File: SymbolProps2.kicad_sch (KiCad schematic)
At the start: 3 parts

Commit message: actually aligned correctly
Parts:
- removed U? (x3): PropsTest, symbol PropLib:PropsTest
- added U? (x12): PropsTest, symbol PropLib:PropsTest
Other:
- note added: "+90"
- note added: "-90"
- note added: "180"
- note added: "MIR X"
- note added: "MIR Y"
- note added: "PLAIN"

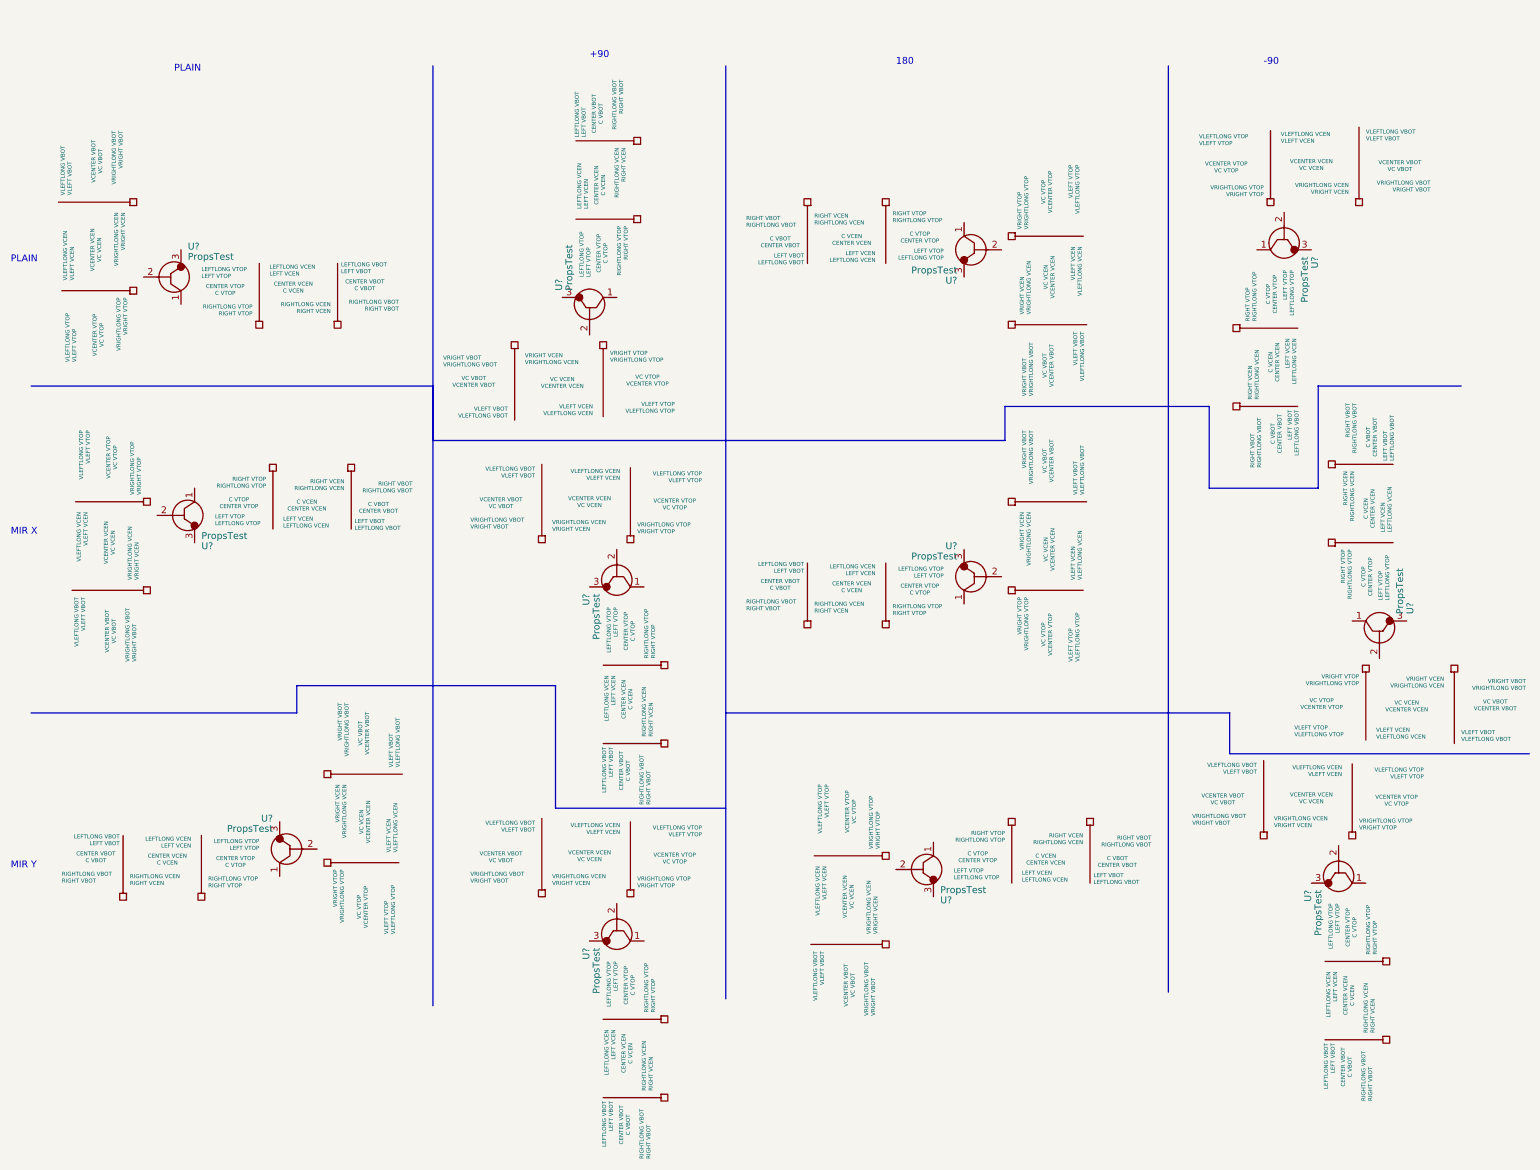
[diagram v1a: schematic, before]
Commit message: add ref annotations
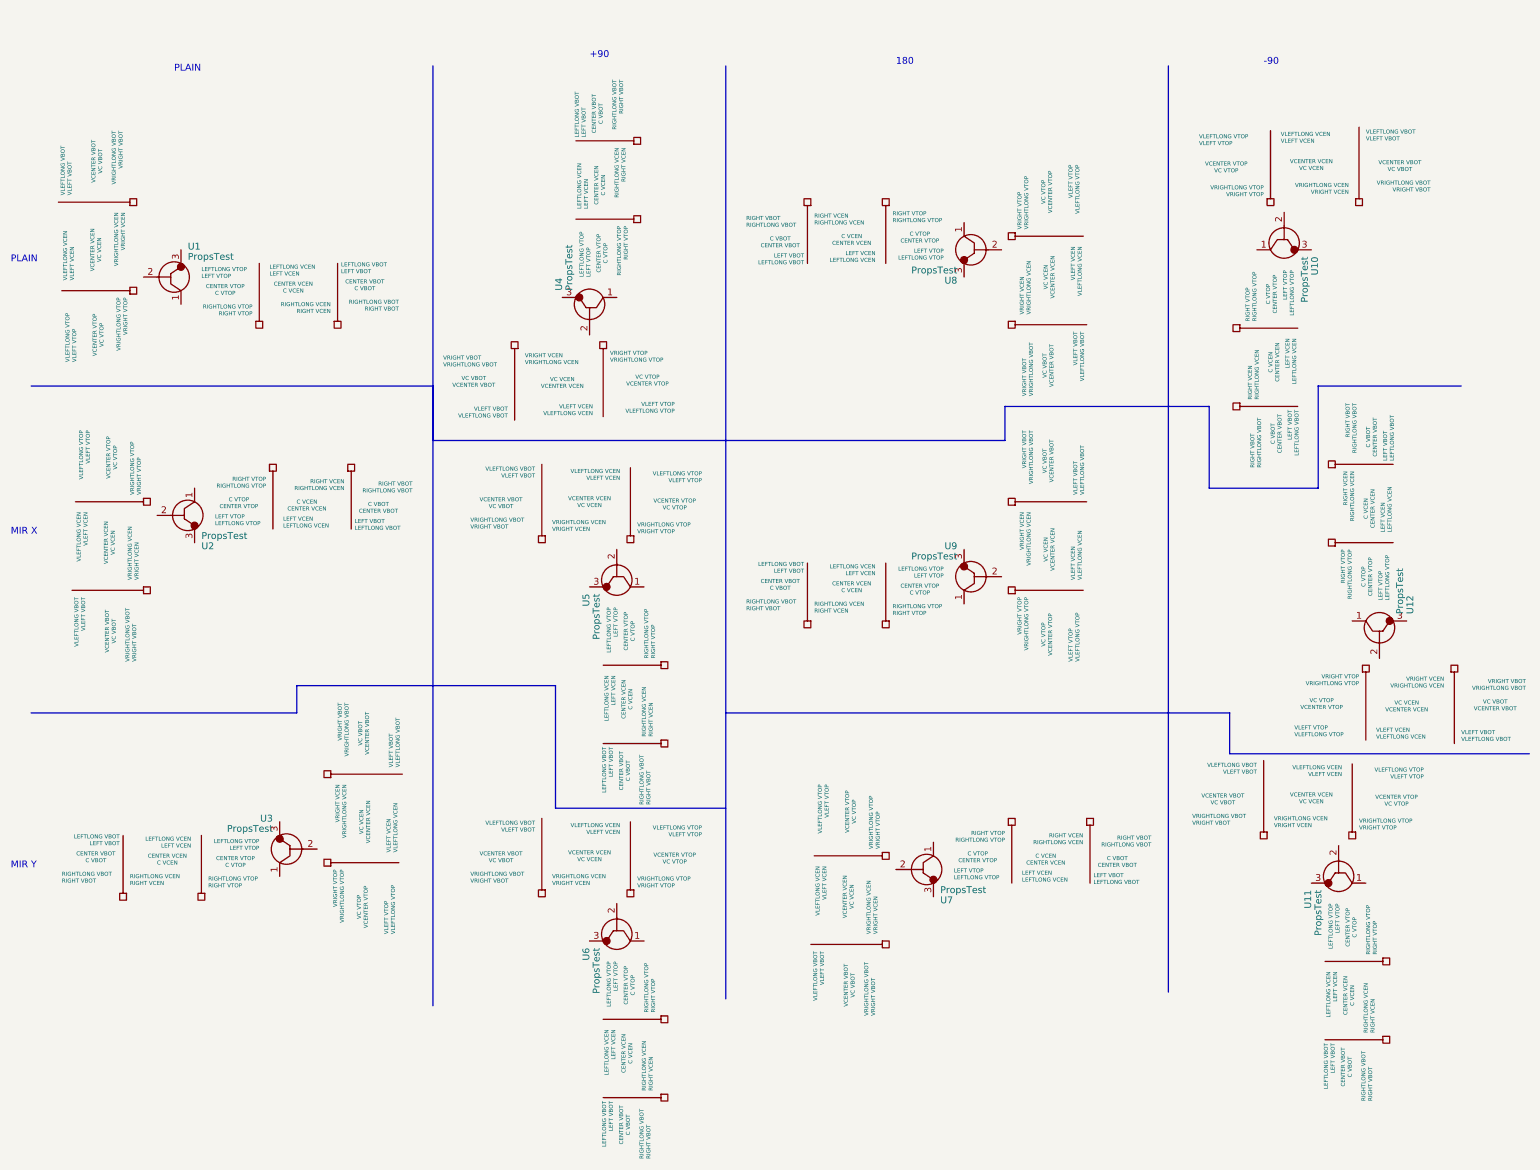
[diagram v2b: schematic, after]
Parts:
- gave numbers to parts that had none: 12
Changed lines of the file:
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@@
   (symbol (lib_id "PropLib:PropsTest") (at 183.515 175.26 0) (mirror x) (unit 1)
     (in_bom yes) (on_board yes)
-    (property "Reference" "U?" (id 0) (at 186.055 175.895 0)
+    (property "Reference" "U7" (id 0) (at 186.055 175.895 0)
       (effects (font (size 1.27 1.27)) (justify left))
     )
@@
   (symbol (lib_id "PropLib:PropsTest") (at 64.135 161.29 0) (mirror y) (unit 1)
     (in_bom yes) (on_board yes)
-    (property "Reference" "U?" (id 0) (at 61.595 160.655 0)
+    (property "Reference" "U3" (id 0) (at 61.595 160.655 0)
       (effects (font (size 1.27 1.27)) (justify left))
     )
@@
   (symbol (lib_id "PropLib:PropsTest") (at 273.05 125.095 270) (mirror x) (unit 1)
     (in_bom yes) (on_board yes)
-    (property "Reference" "U?" (id 0) (at 273.685 122.555 0)
+    (property "Reference" "U12" (id 0) (at 273.685 122.555 0)
       (effects (font (size 1.27 1.27)) (justify left))
     )
@@
   (symbol (lib_id "PropLib:PropsTest") (at 120.65 182.245 90) (mirror x) (unit 1)
     (in_bom yes) (on_board yes)
-    (property "Reference" "U?" (id 0) (at 120.015 184.785 0)
+    (property "Reference" "U6" (id 0) (at 120.015 184.785 0)
       (effects (font (size 1.27 1.27)) (justify left))
     )
@@
   (symbol (lib_id "PropLib:PropsTest") (at 43.18 54.61 0) (unit 1)
     (in_bom yes) (on_board yes)
-    (property "Reference" "U?" (id 0) (at 45.72 53.975 0)
+    (property "Reference" "U1" (id 0) (at 45.72 53.975 0)
       (effects (font (size 1.27 1.27)) (justify left))
     )
@@
   (symbol (lib_id "PropLib:PropsTest") (at 255.27 53.34 270) (unit 1)
     (in_bom yes) (on_board yes)
-    (property "Reference" "U?" (id 0) (at 255.905 55.88 0)
+    (property "Reference" "U10" (id 0) (at 255.905 55.88 0)
       (effects (font (size 1.27 1.27)) (justify left))
     )
@@
   (symbol (lib_id "PropLib:PropsTest") (at 191.77 59.69 180) (unit 1)
     (in_bom yes) (on_board yes)
-    (property "Reference" "U?" (id 0) (at 189.23 60.325 0)
+    (property "Reference" "U8" (id 0) (at 189.23 60.325 0)
       (effects (font (size 1.27 1.27)) (justify left))
     )
@@
   (symbol (lib_id "PropLib:PropsTest") (at 120.65 116.205 90) (mirror x) (unit 1)
     (in_bom yes) (on_board yes)
-    (property "Reference" "U?" (id 0) (at 120.015 118.745 0)
+    (property "Reference" "U5" (id 0) (at 120.015 118.745 0)
       (effects (font (size 1.27 1.27)) (justify left))
     )
@@
   (symbol (lib_id "PropLib:PropsTest") (at 255.27 171.45 90) (mirror x) (unit 1)
     (in_bom yes) (on_board yes)
-    (property "Reference" "U?" (id 0) (at 254.635 173.99 0)
+    (property "Reference" "U11" (id 0) (at 254.635 173.99 0)
       (effects (font (size 1.27 1.27)) (justify left))
     )
@@
   (symbol (lib_id "PropLib:PropsTest") (at 191.77 110.49 0) (mirror y) (unit 1)
     (in_bom yes) (on_board yes)
-    (property "Reference" "U?" (id 0) (at 189.23 109.855 0)
+    (property "Reference" "U9" (id 0) (at 189.23 109.855 0)
       (effects (font (size 1.27 1.27)) (justify left))
     )
@@
   (symbol (lib_id "PropLib:PropsTest") (at 115.57 64.77 90) (unit 1)
     (in_bom yes) (on_board yes)
-    (property "Reference" "U?" (id 0) (at 114.935 62.23 0)
+    (property "Reference" "U4" (id 0) (at 114.935 62.23 0)
       (effects (font (size 1.27 1.27)) (justify left))
     )
@@
   (symbol (lib_id "PropLib:PropsTest") (at 45.72 109.22 0) (mirror x) (unit 1)
     (in_bom yes) (on_board yes)
-    (property "Reference" "U?" (id 0) (at 48.26 109.855 0)
+    (property "Reference" "U2" (id 0) (at 48.26 109.855 0)
       (effects (font (size 1.27 1.27)) (justify left))
     )
@@
   )
   (symbol_instances
+    (path "/607681bc-b8ab-4cc3-bcbe-d5cdf4623d17"
+      (reference "U1") (unit 1) (value "PropsTest") (footprint "")
+    )
+    (path "/d1604d4c-584e-4e63-9761-bccff5ea1220"
+      (reference "U2") (unit 1) (value "PropsTest") (footprint "")
+    )
+    (path "/302a6788-cdde-4eda-bd6a-10393a6c4075"
+      (reference "U3") (unit 1) (value "PropsTest") (footprint "")
+    )
+    (path "/c09b4851-553e-4297-9d60-9ff4a40ae4ee"
+      (reference "U4") (unit 1) (value "PropsTest") (footprint "")
+    )
+    (path "/8722b612-3282-498c-be60-45a7b3205850"
+      (reference "U5") (unit 1) (value "PropsTest") (footprint "")
+    )
+    (path "/5681e071-aff0-4628-ba3c-632cbed13cad"
+      (reference "U6") (unit 1) (value "PropsTest") (footprint "")
+    )
     (path "/29a881e8-06df-4b6b-afb0-3c2df8355293"
-      (reference "U?") (unit 1) (value "PropsTest") (footprint "")
-    )
-    (path "/302a6788-cdde-4eda-bd6a-10393a6c4075"
-      (reference "U?") (unit 1) (value "PropsTest") (footprint "")
+      (reference "U7") (unit 1) (value "PropsTest") (footprint "")
+    )
+    (path "/8285ad37-34fa-4bac-8b4e-ebcb827dd7e3"
+      (reference "U8") (unit 1) (value "PropsTest") (footprint "")
+    )
+    (path "/bd6d4bff-5ad6-4b0b-b3d0-86cdd8ca4399"
+      (reference "U9") (unit 1) (value "PropsTest") (footprint "")
+    )
+    (path "/81611058-008a-4b8d-b0a8-652432d762c0"
+      (reference "U10") (unit 1) (value "PropsTest") (footprint "")
+    )
+    (path "/a431c1e4-6c80-42a2-b56c-6b8cbb3325b1"
+      (reference "U11") (unit 1) (value "PropsTest") (footprint "")
     )
     (path "/3bb5f9d7-3747-4cee-9ede-8fcd24e3d2ab"
-      (reference "U?") (unit 1) (value "PropsTest") (footprint "")
-    )
-    (path "/5681e071-aff0-4628-ba3c-632cbed13cad"
-      (reference "U?") (unit 1) (value "PropsTest") (footprint "")
-    )
-    (path "/607681bc-b8ab-4cc3-bcbe-d5cdf4623d17"
-      (reference "U?") (unit 1) (value "PropsTest") (footprint "")
-    )
-    (path "/81611058-008a-4b8d-b0a8-652432d762c0"
-      (reference "U?") (unit 1) (value "PropsTest") (footprint "")
-    )
-    (path "/8285ad37-34fa-4bac-8b4e-ebcb827dd7e3"
-      (reference "U?") (unit 1) (value "PropsTest") (footprint "")
-    )
-    (path "/8722b612-3282-498c-be60-45a7b3205850"
-      (reference "U?") (unit 1) (value "PropsTest") (footprint "")
-    )
-    (path "/a431c1e4-6c80-42a2-b56c-6b8cbb3325b1"
-      (reference "U?") (unit 1) (value "PropsTest") (footprint "")
-    )
-    (path "/bd6d4bff-5ad6-4b0b-b3d0-86cdd8ca4399"
-      (reference "U?") (unit 1) (value "PropsTest") (footprint "")
-    )
-    (path "/c09b4851-553e-4297-9d60-9ff4a40ae4ee"
-      (reference "U?") (unit 1) (value "PropsTest") (footprint "")
-    )
-    (path "/d1604d4c-584e-4e63-9761-bccff5ea1220"
-      (reference "U?") (unit 1) (value "PropsTest") (footprint "")
+      (reference "U12") (unit 1) (value "PropsTest") (footprint "")
     )
   )

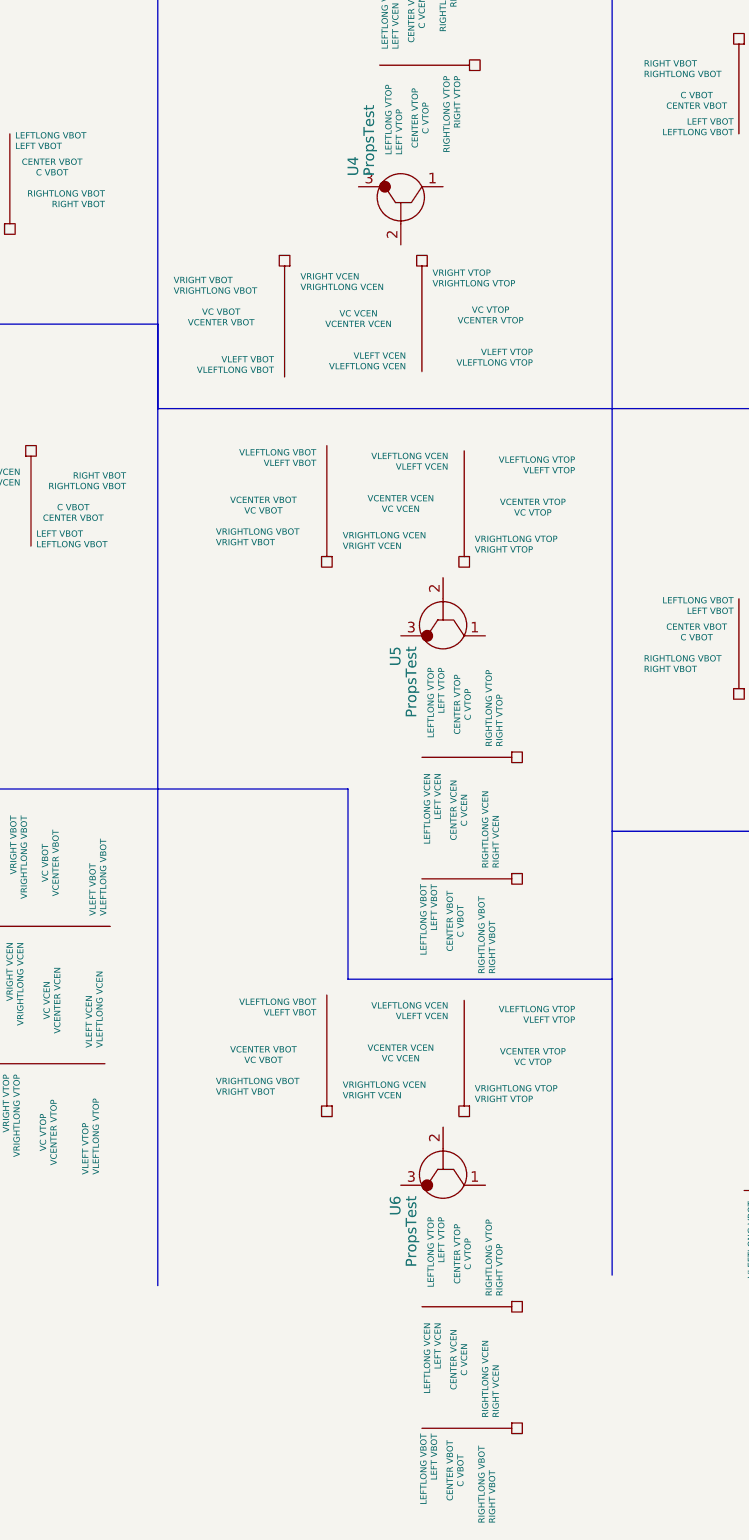
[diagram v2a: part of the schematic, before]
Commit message: fix some orientation
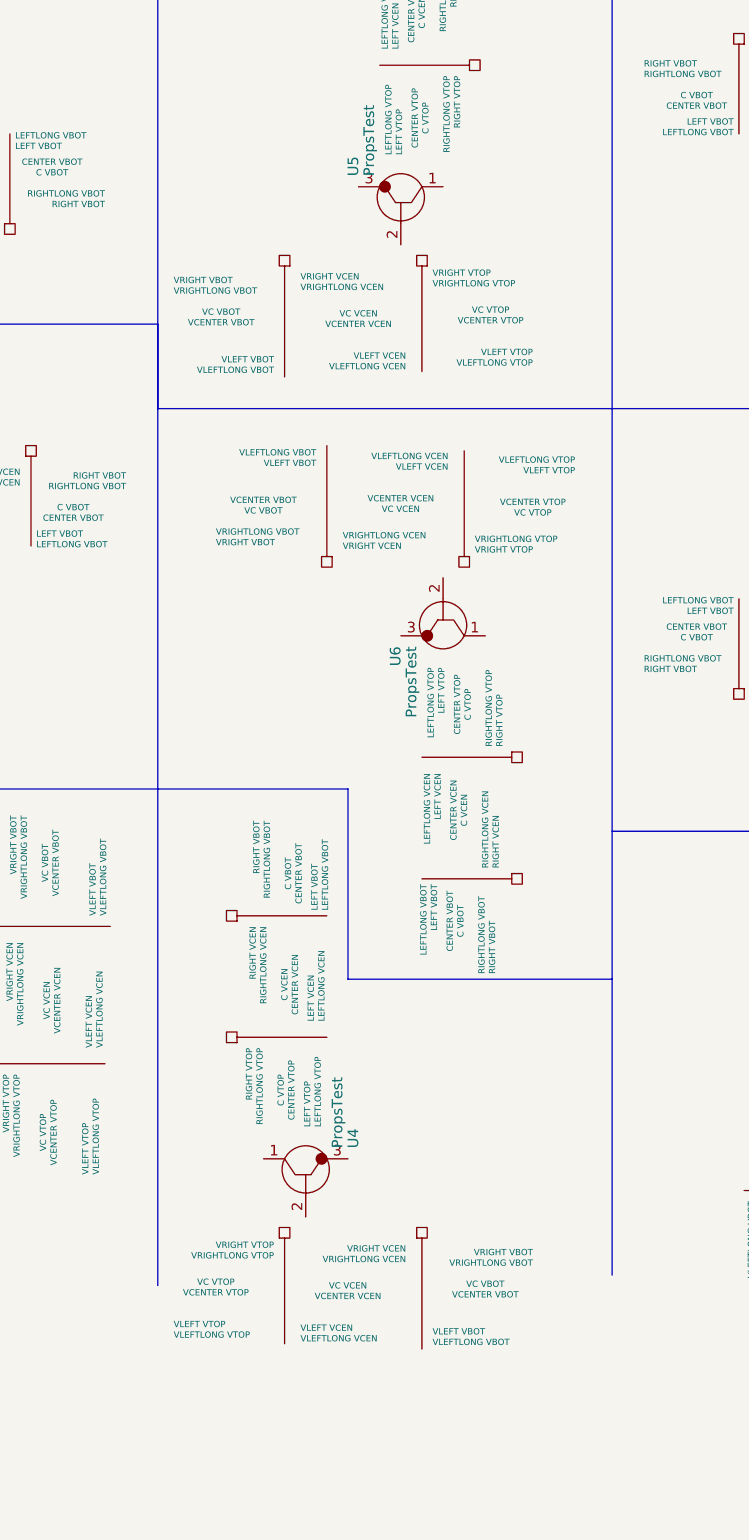
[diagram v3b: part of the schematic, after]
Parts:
- renumbered U6 to U4, U4 to U5, U5 to U6
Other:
- moved on the sheet: U4
